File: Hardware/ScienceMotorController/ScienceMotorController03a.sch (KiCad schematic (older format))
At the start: 17 parts, among them U8 VNH5019A_E

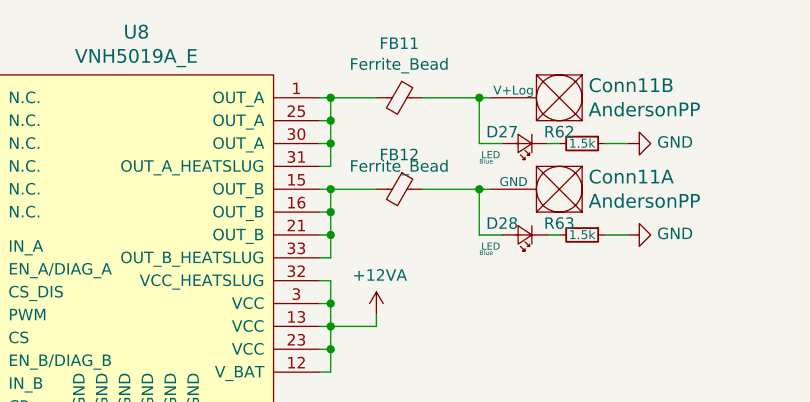
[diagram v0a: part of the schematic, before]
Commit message: finished assigning footprints, generated pcbnew
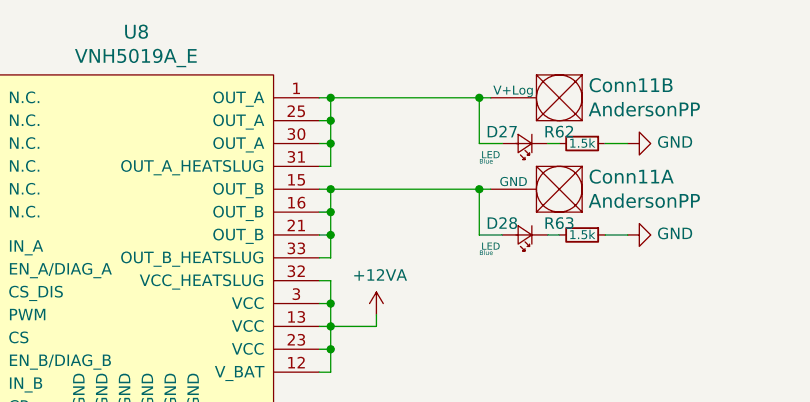
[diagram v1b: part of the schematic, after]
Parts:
- removed FB11, FB12: Ferrite_Bead, symbol Device:Ferrite_Bead_Small
- U8: footprint (none) -> MRDT_ICs:MultiPowerSO_30
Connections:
- net at Conn11.2 (V+Log), D27.2 (A): now also U8.1 (OUT_A), U8.25 (OUT_A), U8.30 (OUT_A), U8.31 (OUT_A_HEATSLUG)
- net at Conn11.1 (GND), D28.2 (A): now also U8.15 (OUT_B), U8.16 (OUT_B), U8.21 (OUT_B), U8.33 (OUT_B_HEATSLUG)
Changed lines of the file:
@@
 F 0 "U8" H 5850 5837 60  0000 C CNN
 F 1 "VNH5019A_E" H 5850 5731 60  0000 C CNN
-F 2 "" H 5250 5450 60  0001 C CNN
+F 2 "MRDT_ICs:MultiPowerSO_30" H 5250 5450 60  0001 C CNN
 F 3 "" H 5250 5450 60  0001 C CNN
 	1    5250 4150
@@
 Connection ~ 4100 3800
 Wire Wire Line
-	7100 2750 7350 2750
-Wire Wire Line
-	7100 3150 7350 3150
-Wire Wire Line
 	7350 2950 7350 2750
 Connection ~ 7350 2750
@@
 	1    0    0    -1
 $EndComp
-$Comp
-L Device:Ferrite_Bead_Small FB?
-U 1 1 5F9C1894
-P 7000 2750
-AR Path="/5F9082F6/5F9C1894" Ref="FB?"  Part="1"
-AR Path="/5F7148FA/5FA34AD3/5F9C1894" Ref="FB11"  Part="1"
-F 0 "FB11" V 6763 2750 50  0000 C CNN
-F 1 "Ferrite_Bead" V 6854 2750 50  0000 C CNN
-F 2 "" V 6930 2750 50  0001 C CNN
-F 3 "~" H 7000 2750 50  0001 C CNN
-	1    7000 2750
-	0    1    1    0
-$EndComp
-$Comp
-L Device:Ferrite_Bead_Small FB?
-U 1 1 5F9C2846
-P 7000 3150
-AR Path="/5F9082F6/5F9C2846" Ref="FB?"  Part="1"
-AR Path="/5F7148FA/5FA34AD3/5F9C2846" Ref="FB12"  Part="1"
-F 0 "FB12" V 6850 3150 50  0000 C CNN
-F 1 "Ferrite_Bead" V 6900 3150 50  0000 C CNN
-F 2 "" V 6930 3150 50  0001 C CNN
-F 3 "~" H 7000 3150 50  0001 C CNN
-	1    7000 3150
-	0    1    1    0
-$EndComp
-Wire Wire Line
-	6900 2750 6700 2750
 Connection ~ 6700 2750
-Wire Wire Line
-	6900 3150 6700 3150
 Connection ~ 6700 3150
 Text HLabel 4600 3400 0    50   Input ~ 0
@@
 Text Notes 7350 3450 0    20   ~ 0
 Blue
+Wire Wire Line
+	6700 2750 7350 2750
+Wire Wire Line
+	6700 3150 7350 3150
 $EndSCHEMATC

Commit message: began placing footprints on layout
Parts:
- Conn11: footprint MRDT_Connectors:Anderson_2_Vertical_Sidy_by_Side -> MRDT_Connectors:Anderson_2_Horizontal_Side_by_Side
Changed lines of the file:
@@
 F 0 "Conn11" H 7772 3097 60  0000 R CNN
 F 1 "AndersonPP" H 7772 3203 60  0000 R CNN
-F 2 "MRDT_Connectors:Anderson_2_Vertical_Sidy_by_Side" H 7650 2500 60  0001 C CNN
+F 2 "MRDT_Connectors:Anderson_2_Horizontal_Side_by_Side" H 7650 2500 60  0001 C CNN
 F 3 "" H 7650 2500 60  0001 C CNN
 	1    7800 3050
@@
 F 0 "Conn11" H 7772 2697 60  0000 R CNN
 F 1 "AndersonPP" H 7772 2803 60  0000 R CNN
-F 2 "MRDT_Connectors:Anderson_2_Vertical_Sidy_by_Side" H 7650 2100 60  0001 C CNN
+F 2 "MRDT_Connectors:Anderson_2_Horizontal_Side_by_Side" H 7650 2100 60  0001 C CNN
 F 3 "" H 7650 2100 60  0001 C CNN
 	2    7800 2650

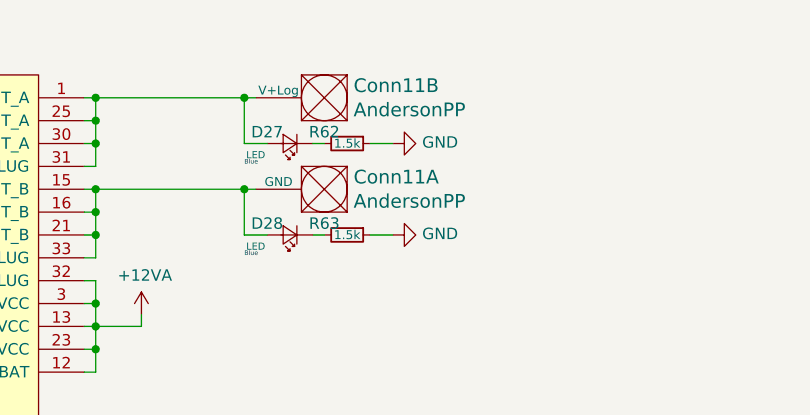
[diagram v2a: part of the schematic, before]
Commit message: running traces
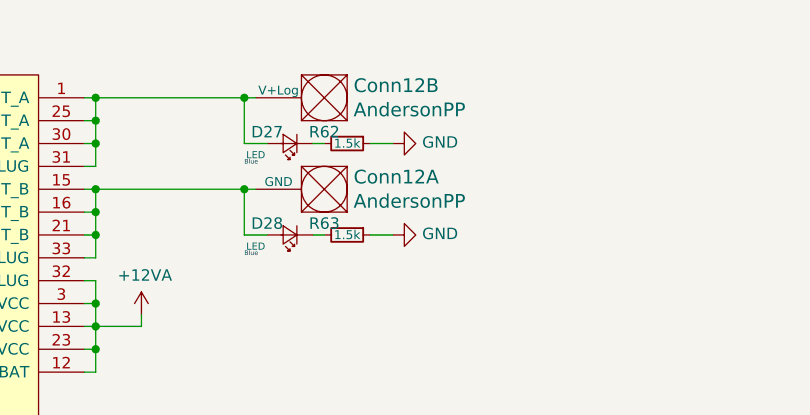
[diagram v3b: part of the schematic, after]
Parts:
- renumbered Conn11 to Conn12
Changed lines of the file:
@@
 AR Path="/5F7D111E/5FA0F855/5FA34915" Ref="Conn?"  Part="1"
 AR Path="/5F9082F6/5FA34915" Ref="Conn?"  Part="1"
-AR Path="/5F7148FA/5FA34AD3/5FA34915" Ref="Conn11"  Part="1"
-F 0 "Conn11" H 7772 3097 60  0000 R CNN
+AR Path="/5F7148FA/5FA34AD3/5FA34915" Ref="Conn12"  Part="1"
+F 0 "Conn12" H 7772 3097 60  0000 R CNN
 F 1 "AndersonPP" H 7772 3203 60  0000 R CNN
 F 2 "MRDT_Connectors:Anderson_2_Horizontal_Side_by_Side" H 7650 2500 60  0001 C CNN
@@
 AR Path="/5F7D111E/5FA0F855/5FA3491B" Ref="Conn?"  Part="2"
 AR Path="/5F9082F6/5FA3491B" Ref="Conn?"  Part="2"
-AR Path="/5F7148FA/5FA34AD3/5FA3491B" Ref="Conn11"  Part="2"
-F 0 "Conn11" H 7772 2697 60  0000 R CNN
+AR Path="/5F7148FA/5FA34AD3/5FA3491B" Ref="Conn12"  Part="2"
+F 0 "Conn12" H 7772 2697 60  0000 R CNN
 F 1 "AndersonPP" H 7772 2803 60  0000 R CNN
 F 2 "MRDT_Connectors:Anderson_2_Horizontal_Side_by_Side" H 7650 2100 60  0001 C CNN
